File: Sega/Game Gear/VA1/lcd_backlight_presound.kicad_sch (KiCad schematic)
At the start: 81 parts, among them IC4 uPC356, M5 TestPoint_Small, Q10 2sa812, Q11 2sc1623, Q3 2sd1614, Q4 2sd1614, Q5 2sc1623, Q6 2sc1623, Q7 2sc1623, Q8 2sa812, Q9 2sc1623, T1 Transformer_GG

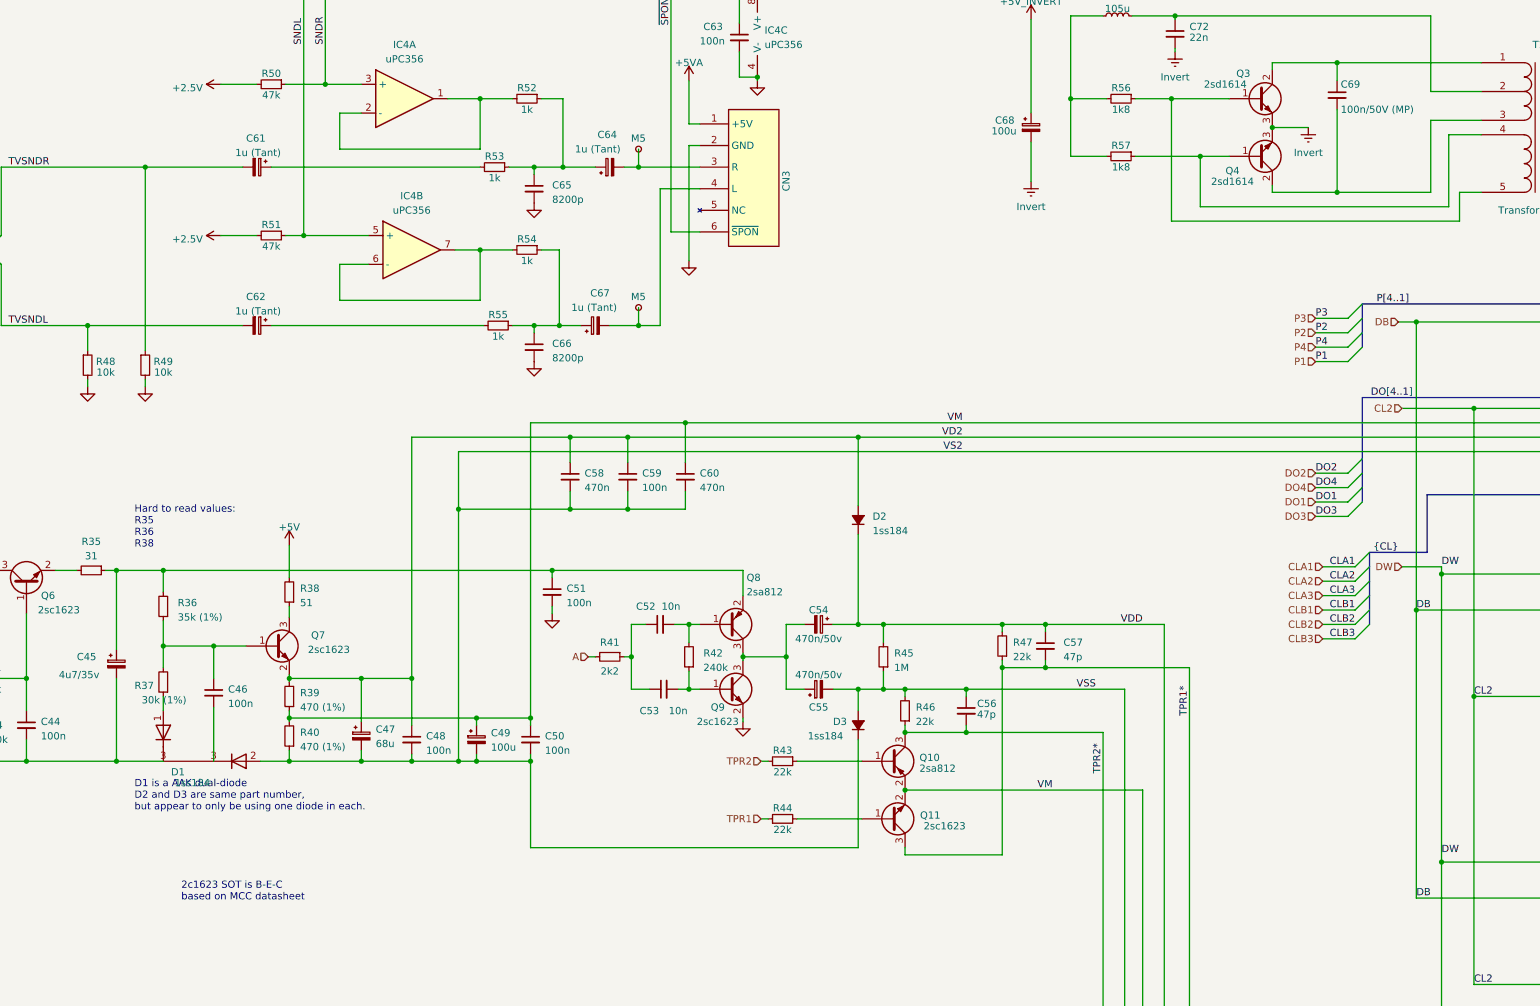
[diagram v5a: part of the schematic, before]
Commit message: GG VA1 passes ERC, needs review
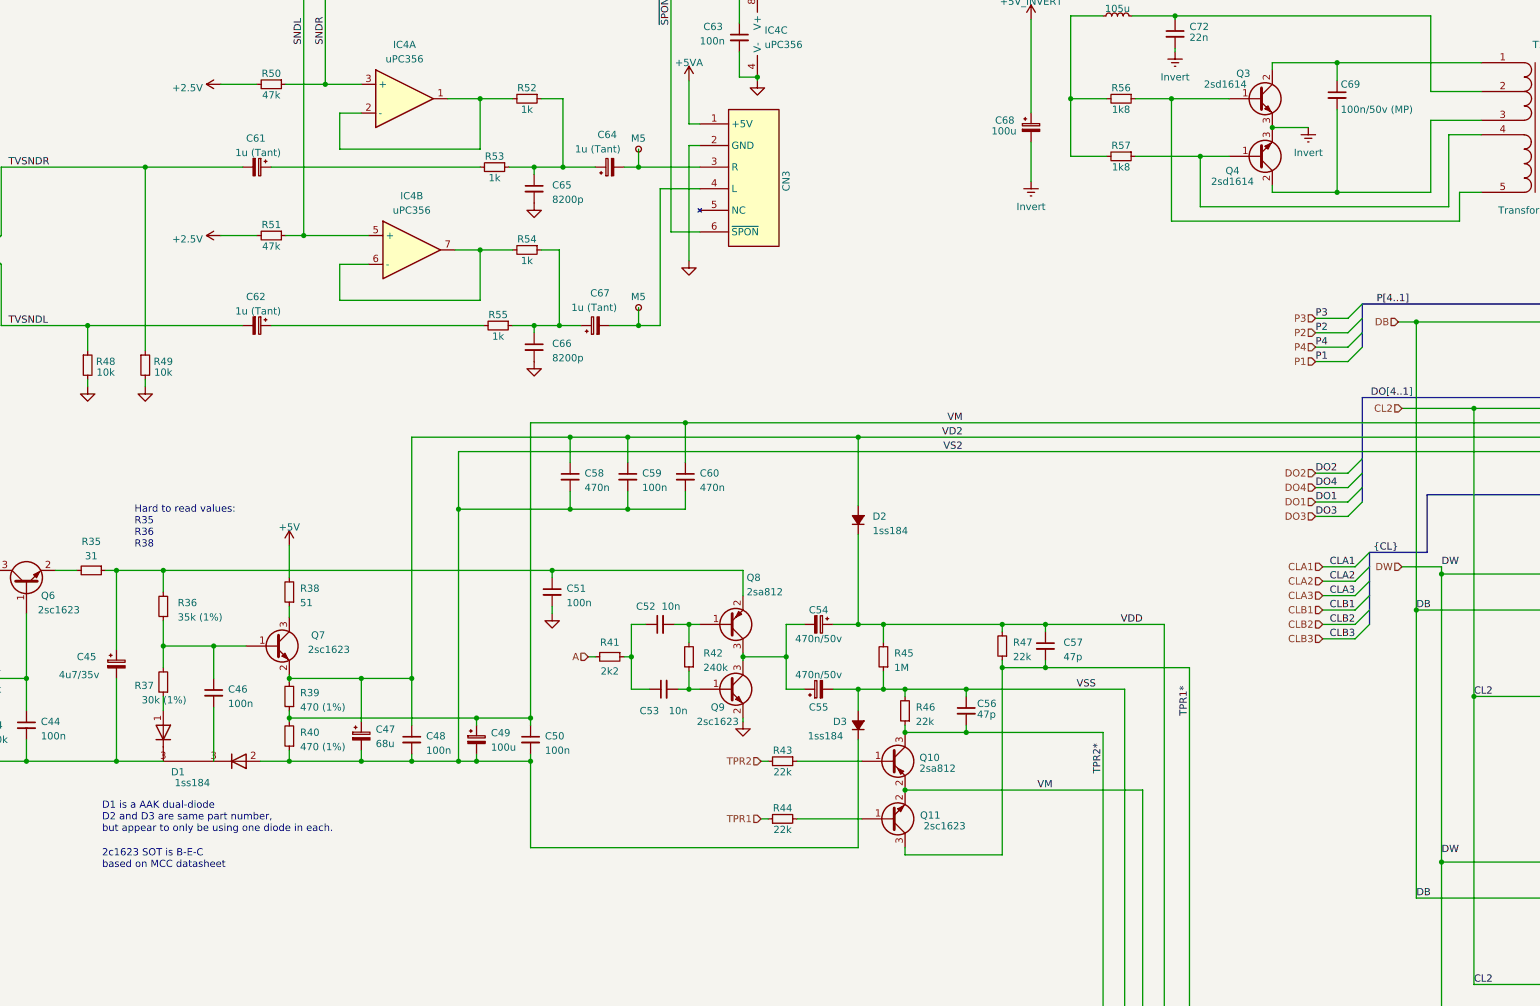
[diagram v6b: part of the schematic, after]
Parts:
- C69: value 100n/50V (MP) -> 100n/50v (MP)
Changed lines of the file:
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@@
   (title_block
     (title "LCD Connection")
+    (date "2023-02-07")
+    (rev "1")
+    (comment 1 "bald.ee/bitpreserve")
+    (comment 2 "Drawn by James Lewis (@baldengineer)")
   )
   (bus_alias "" (members ))
@@
   )
   (text "NCs are connected to GND\nin OG schematic." (at 381.635 65.405 0)
-    (effects (font (size 1.27 1.27)) (justify left bottom))
+    (effects (font (face "Verdana") (size 1.27 1.27)) (justify left bottom))
   )
-  (text "2c1623 SOT is B-E-C\nbased on MCC datasheet" (at 89.535 181.61 0)
-    (effects (font (size 1.27 1.27)) (justify left bottom))
+  (text "2c1623 SOT is B-E-C\nbased on MCC datasheet" (at 75.565 175.895 0)
+    (effects (font (face "Verdana") (size 1.27 1.27)) (justify left bottom))
   )
   (text "D1 is a AAK dual-diode\nD2 and D3 are same part number, \nbut appear to only be using one diode in each."
-    (at 81.28 165.735 0)
-    (effects (font (size 1.27 1.27)) (justify left bottom))
+    (at 75.565 169.545 0)
+    (effects (font (face "Verdana") (size 1.27 1.27)) (justify left bottom))
   )
   (text "Hard to read values:\nR35\nR36\nR38" (at 81.28 119.38 0)
-    (effects (font (size 1.27 1.27)) (justify left bottom))
+    (effects (font (face "Verdana") (size 1.27 1.27)) (justify left bottom))
   )
   (label "CLA1" (at 354.33 109.855 0) (fields_autoplaced)
@@
       (effects (font (size 1.27 1.27)) (justify left))
     )
-    (property "Value" "100n/50V (MP)" (at 294.005 41.91 0)
+    (property "Value" "100n/50v (MP)" (at 294.005 41.91 0)
       (effects (font (size 1.27 1.27)) (justify left))
     )
